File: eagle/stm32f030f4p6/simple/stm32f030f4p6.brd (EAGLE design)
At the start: 160 x 100 mm, 16 parts

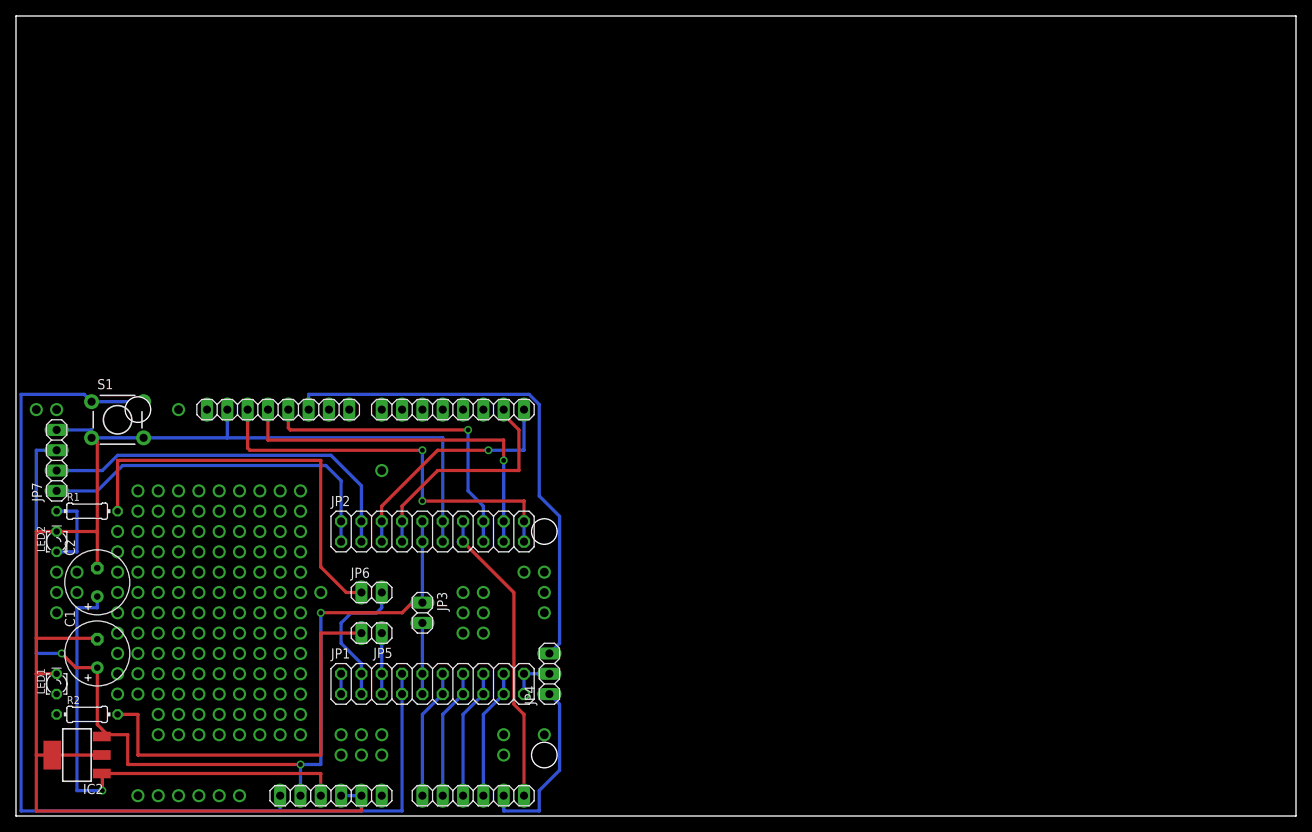
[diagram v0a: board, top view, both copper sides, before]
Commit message: Dimensions fixes
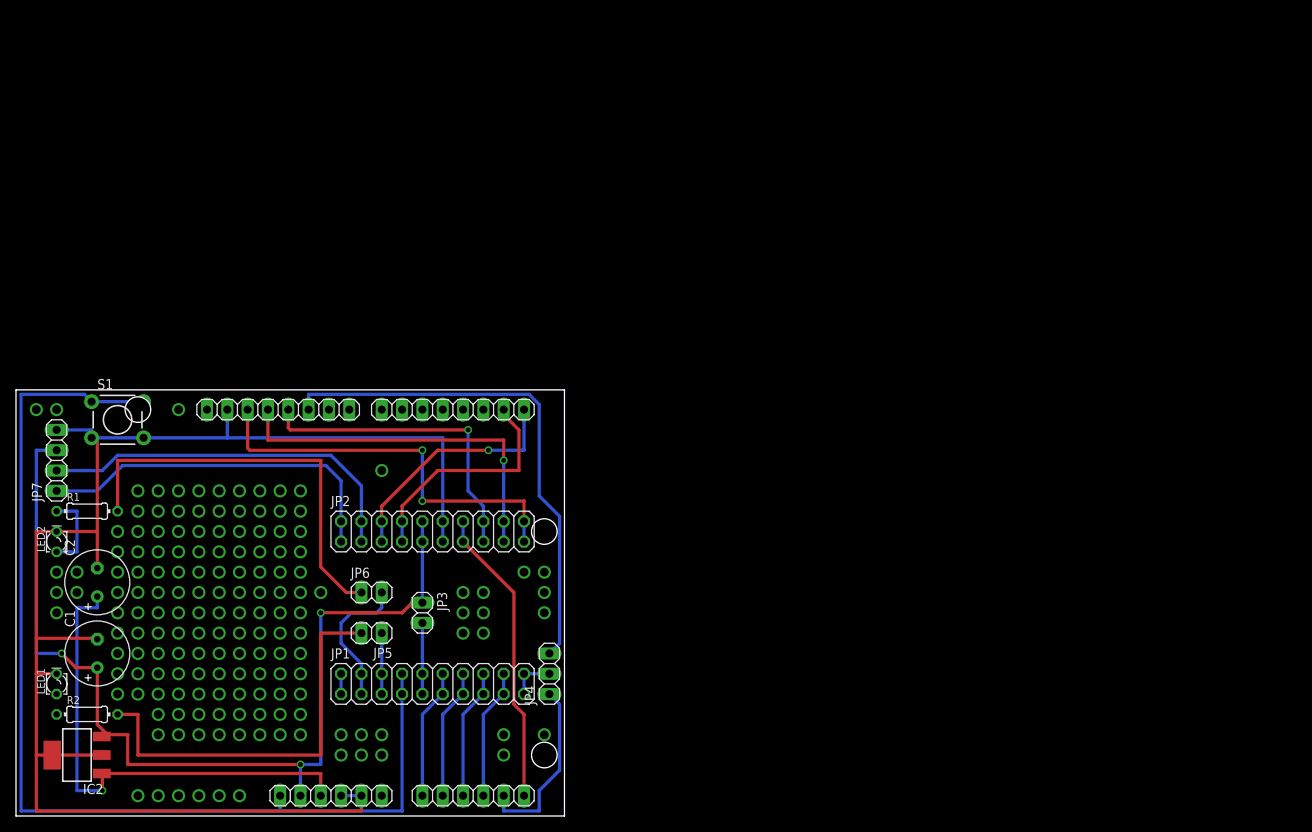
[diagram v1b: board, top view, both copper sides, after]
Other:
- board size 160 x 100 mm -> 68.6 x 53.3 mm
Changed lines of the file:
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@@
 <setting verticaltext="up"/>
 </settings>
-<grid distance="0.1" unitdist="inch" unit="inch" style="lines" multiple="1" display="yes" altdistance="0.0125" altunitdist="inch" altunit="inch"/>
+<grid distance="0.01" unitdist="inch" unit="inch" style="lines" multiple="1" display="yes" altdistance="0.0125" altunitdist="inch" altunit="inch"/>
 <layers>
 <layer number="1" name="Top" color="4" fill="1" visible="yes" active="yes"/>
@@
 <board>
 <plain>
-<wire x1="0" y1="0" x2="160" y2="0" width="0" layer="20"/>
-<wire x1="160" y1="0" x2="160" y2="100" width="0" layer="20"/>
-<wire x1="160" y1="100" x2="0" y2="100" width="0" layer="20"/>
-<wire x1="0" y1="100" x2="0" y2="0" width="0" layer="20"/>
+<wire x1="0" y1="0" x2="68.56" y2="0" width="0" layer="20"/>
+<wire x1="68.56" y1="0" x2="68.56" y2="53.264" width="0" layer="20"/>
+<wire x1="68.56" y1="53.264" x2="0" y2="53.264" width="0" layer="20"/>
+<wire x1="0" y1="53.264" x2="0" y2="0" width="0" layer="20"/>
 </plain>
 <attributes>
